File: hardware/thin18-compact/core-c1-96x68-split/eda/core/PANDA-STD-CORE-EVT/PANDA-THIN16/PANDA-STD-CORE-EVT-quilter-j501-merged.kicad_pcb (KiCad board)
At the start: 4 copper layers, 96 x 68 mm, 147 parts, among them J201 U20405-01 USB2.0, J301 HC-HY-2AWT, J302 HC-1.0-3PWT NTC, J501 TF-122-CCP9 / microSD, J502 HC-1.0-2PWT BTL, J503 TC2030-IDC-NL / DEBUG, J601 HC-PBB40C-60DS-0.4V-1.5-02, J803 X05A10H06G, J804 X05A10H06G, SW201 TS-1186E-B-B, SW202 TS-1186E-B-B, U302 SD3078, U402 SGM2578SDYG/TR, U403 SGM2578SDYG/TR, U404 SGM2578SDYG/TR, U405 SGM2578SDYG/TR, U501 ESP32-S3-WROOM-1U-N16R8, U503 QMI8658A, U601 XL9535, U901 SGM41513YTQF24G/TR, U902 SGM62125AXG/TR, U903 CW2217BAAD, U904 NS4168, U905 SGM37601YTRL20G/TR

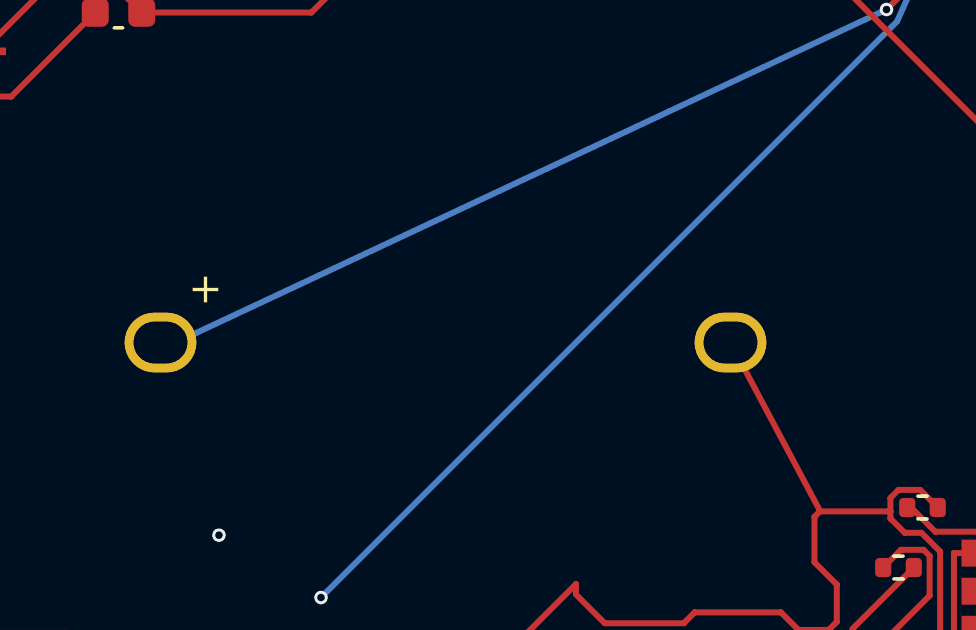
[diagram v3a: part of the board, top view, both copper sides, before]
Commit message: fix(hardware): use exact H3C capacitor with 20mm leads
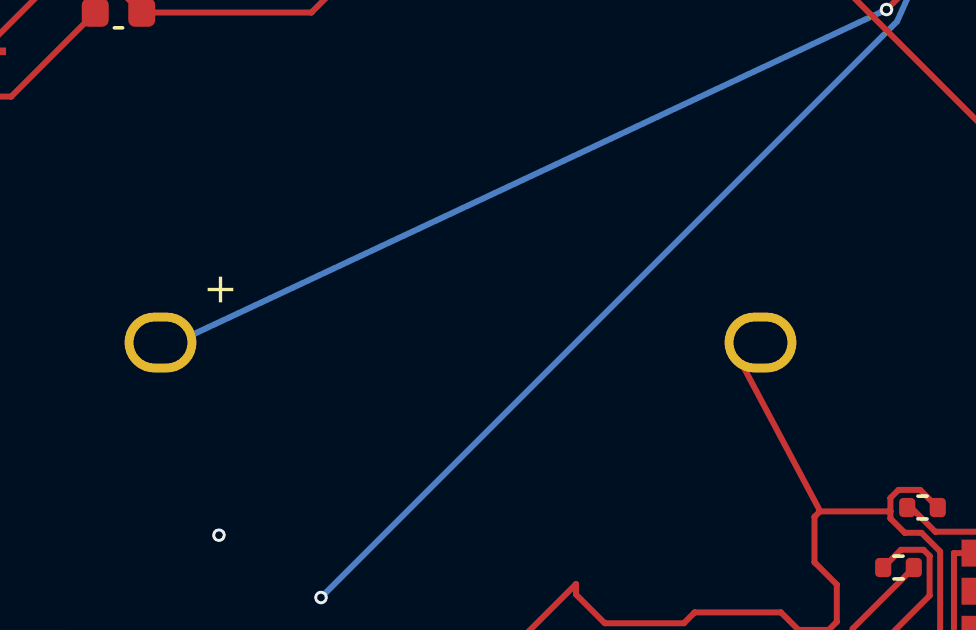
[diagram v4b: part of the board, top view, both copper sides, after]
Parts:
- C301: value SE-5R5-D105VYH -> SE-5R5-D105VYH3C; footprint panda-standard:KAMCAP_SE5R5_D105VYH -> panda-standard:KAMCAP_SE5R5_D105VYH3C
- moved C301 0.50 mm to (59.4, 43.5)
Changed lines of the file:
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@@
 (property "LCSC" "C22399626" (at 0 0 0) (layer "F.Fab") (hide yes) (effects (font (size 1.27 1.27))))(property "Manufacturer" "HRE" (at 0 0 0) (layer "F.Fab") (hide yes) (effects (font (size 1 1))))(property "MPN" "CGA0603X7R106K100JT" (at 0 0 0) (layer "F.Fab") (hide yes) (effects (font (size 1 1)))) (property "Description" "Controlled prototype ECO: HRE 10uF 10V X7R +/-10% 0603, C22399626; effective DC-bias capacitance remains a physical qualification item." (at 0 0 0) (layer "F.Fab") (hide yes) (effects (font (size 1.27 1.27)))) (property "KiLib_Generator" "SMD_2terminal_chip_molded" (at 0 0 0) (layer "F.SilkS") (hide yes) (effects (font (size 1 1) (thickness 0.15)))) (attr smd) (duplicate_pad_numbers_are_jumpers no) (fp_line (start -0.14058 -0.51) (end 0.14058 -0.51) (stroke (width 0.12) (type solid)) (layer "F.SilkS")) (fp_line (start -0.14058 0.51) (end 0.14058 0.51) (stroke (width 0.12) (type solid)) (layer "F.SilkS")) (fp_rect (start -1.48 -0.73) (end 1.48 0.73) (stroke (width 0.05) (type solid)) (fill no) (layer "F.CrtYd")) (fp_rect (start -0.8 -0.4) (end 0.8 0.4) (stroke (width 0.1) (type solid)) (fill no) (layer "F.Fab")) (fp_text user "${REFERENCE}" (at 0 0 0) (layer "F.Fab") (effects (font (size 0.4 0.4) (thickness 0.06)))) (pad "1" smd roundrect (at -0.775 0) (size 0.9 0.95) (layers "F.Cu" "F.Mask" "F.Paste") (roundrect_rratio 0.25) (net "3V3_SD")) (pad "2" smd roundrect (at 0.775 0) (size 0.9 0.95) (layers "F.Cu" "F.Mask" "F.Paste") (roundrect_rratio 0.25) (net "GND")) (embedded_fonts no) (model "${KICAD10_3DMODEL_DIR}/Capacitor_SMD.3dshapes/C_0603_1608Metric.step" (offset (xyz 0 0 0)) (scale (xyz 1 1 1)) (rotate (xyz 0 0 0))))
 	(footprint "Capacitor_SMD:C_0402_1005Metric" (locked yes) (layer "F.Cu") (at 44.75 15.25 -90) (descr "Capacitor SMD 0402 (1005 Metric), square (rectangular) end terminal, IPC-7351 nominal, (Body size source: IPC-SM-782 page 76, https://www.pcb-3d.com/wordpress/wp-content/uploads/ipc-sm-782a_amendment_1_and_2.pdf)") (tags "capacitor") (property "Reference" "C303" (at 0 1.8 90) (layer "F.SilkS") (hide yes) (effects (font (size 0.8 0.8) (thickness 0.12)))) (property "Value" "1u / BQ BAT" (at 0 1.16 90) (layer "F.Fab") (hide yes) (effects (font (size 1 1) (thickness 0.15)))) (property "Datasheet" "https://www.ti.com/lit/ds/symlink/bq27427.pdf" (at 0 0 90) (layer "F.Fab") (hide yes) (effects (font (size 1.27 1.27))))(property "Manufacturer" "FH (Fenghua Advanced)" (at 0 0 90) (layer "F.Fab") (hide yes) (effects (font (size 1 1))))(property "MPN" "0402B105K100NT" (at 0 0 90) (layer "F.Fab") (hide yes) (effects (font (size 1 1))))(property "LCSC" "C1526" (at 0 0 90) (layer "F.Fab") (hide yes) (effects (font (size 1 1)))) (property "Description" "BQ27427 BAT local ceramic bypass; 1 uF follows TI Table 4-1 and application sections; exact MPN, voltage and DC-bias pending controlled BOM review." (at 0 0 90) (layer "F.Fab") (hide yes) (effects (font (size 1.27 1.27)))) (property "KiLib_Generator" "SMD_2terminal_chip_molded" (at 0 0 90) (layer "F.SilkS") (hide yes) (effects (font (size 1 1) (thickness 0.15)))) (sheetname "/") (sheetfile "PANDA-STD-CORE-EVT.kicad_sch") (attr smd) (duplicate_pad_numbers_are_jumpers no) (fp_line (start -0.107836 0.36) (end 0.107836 0.36) (stroke (width 0.12) (type solid)) (layer "F.SilkS")) (fp_line (start -0.107836 -0.36) (end 0.107836 -0.36) (stroke (width 0.12) (type solid)) (layer "F.SilkS")) (fp_rect (start -0.91 -0.46) (end 0.91 0.46) (stroke (width 0.05) (type solid)) (fill no) (layer "F.CrtYd")) (fp_rect (start -0.5 -0.25) (end 0.5 0.25) (stroke (width 0.1) (type solid)) (fill no) (layer "F.Fab")) (fp_text user "${REFERENCE}" (at 0 0 90) (layer "F.Fab") (effects (font (size 0.25 0.25) (thickness 0.04)))) (pad "1" smd roundrect (at -0.48 0 270) (size 0.56 0.62) (layers "F.Cu" "F.Mask" "F.Paste") (roundrect_rratio 0.25) (net "BAT_PACKP")) (pad "2" smd roundrect (at 0.48 0 270) (size 0.56 0.62) (layers "F.Cu" "F.Mask" "F.Paste") (roundrect_rratio 0.25) (net "GND")) (embedded_fonts no) (model "${KICAD10_3DMODEL_DIR}/Capacitor_SMD.3dshapes/C_0402_1005Metric.step" (offset (xyz 0 0 0)) (scale (xyz 1 1 1)) (rotate (xyz 0 0 0))))
-	(footprint "panda-standard:KAMCAP_SE5R5_D105VYH" (locked yes) (layer "F.Cu") (at 58.9 43.5) (descr "KAMCAP SE-5R5-D105VYH primary2017:1F -20/+80%,5.5V,15ohm maxESR;maxbody19.2diameter/6.0height;leadpitch19+/-0.5,lead1.0+/-0.1. Engineering19mm pitch,platedslots1.8x1.4,lands2.4x2.0. Pin1=positive,2=GND:install actual marked+ terminal on PCB+;drawing has no numbered polarity view. Hand-solder after SMT;body must clear PCB0.2,cut lead belowCore B<=0.5. Prototype retention budget conditional on precharge/current;not physical validation.") (tags "KAMCAP SE-5R5-D105VYH horizontal THT rechargeable RTC backup") (property "Reference" "C301" (at 2.5 -12.3 90) (layer "F.SilkS") (hide yes) (effects (font (size 1 1) (thickness 0.15)))) (property "Value" "SE-5R5-D105VYH" (at 2.5 12.3 90) (layer "F.Fab") (effects (font (size 1 1) (thickness 0.15)))) (property "Datasheet" "https://atta.szlcsc.com/upload/public/pdf/source/20170717/C118887_1500269960558820748.pdf" (at 0 0 90) (layer "B.Fab") (hide yes) (effects (font (size 1.27 1.27))))
-(property "LCSC" "C118887" (at 0 0 90) (layer "B.Fab") (hide yes) (effects (font (size 1.27 1.27))))(property "Manufacturer" "KAMCAP" (at 0 0 90) (layer "B.Fab") (hide yes) (effects (font (size 1 1))))(property "MPN" "SE-5R5-D105VYH" (at 0 0 90) (layer "B.Fab") (hide yes) (effects (font (size 1 1)))) (property "Description" "KAMCAP SE-5R5-D105VYH primary2017:1F -20/+80%,5.5V,15ohm maxESR;maxbody19.2diameter/6.0height;leadpitch19+/-0.5,lead1.0+/-0.1. Engineering19mm pitch,platedslots1.8x1.4,lands2.4x2.0. Pin1=positive,2=GND:install actual marked+ terminal on PCB+;drawing has no numbered polarity view. Hand-solder after SMT;body must clear PCB0.2,cut lead belowCore B<=0.5. Prototype retention budget conditional on precharge/current;not physical validation." (at 0 0 90) (layer "B.Fab") (hide yes) (effects (font (size 1.27 1.27)))) (property "KiLib_Generator" "SMD_2terminal_chip_molded" (at 0 0 90) (layer "F.SilkS") (hide yes) (effects (font (size 1 1) (thickness 0.15)))) (attr through_hole) (duplicate_pad_numbers_are_jumpers no)        (embedded_fonts no)
-(fp_rect (start -10.95 -9.85) (end 10.95 9.85) (stroke (width 0.05) (type solid)) (fill no) (layer "F.CrtYd"))
+	(footprint "panda-standard:KAMCAP_SE5R5_D105VYH3C" (locked yes) (layer "F.Cu") (at 59.4 43.5) (descr "KAMCAP SE-5R5-D105VYH3C primaryJune2020 p3-4:1F 0/+30% at4.4..2.75V,5.5V,15ohm maxAC ESR;maxbody19.2diameter/6.5height;pitch20+/-0.5;flatleads width1.0+/-0.1,thickness0.2+/-0.05. Engineering20mm pitch,platedslots1.8x1.4,lands2.4x2.0. Pin1=positive,2=GND;marked negative terminal to pad2,other positive to PCB+. Post-SMT manual solder only;primary260C<=5s based1.6mm PCB,0.8mmCore process needs qualification;bodyclearance0.2,trimrearleads<=0.5. Conditional24h budget;leakage/low-voltage capacitance/physical EVT not qualified.") (tags "KAMCAP SE-5R5-D105VYH3C horizontal THT rechargeable RTC backup") (property "Reference" "C301" (at 2.5 -12.3 90) (layer "F.SilkS") (hide yes) (effects (font (size 1 1) (thickness 0.15)))) (property "Value" "SE-5R5-D105VYH3C" (at 2.5 12.3 90) (layer "F.Fab") (effects (font (size 1 1) (thickness 0.15)))) (property "Datasheet" "https://atta.szlcsc.com/upload/public/pdf/source/20210914/37A5D1176C23A52D8BA2A343DB47BCB6.pdf" (at 0 0 90) (layer "B.Fab") (hide yes) (effects (font (size 1.27 1.27))))
+(property "LCSC" "C2894294" (at 0 0 90) (layer "B.Fab") (hide yes) (effects (font (size 1.27 1.27))))(property "Manufacturer" "KAMCAP" (at 0 0 90) (layer "B.Fab") (hide yes) (effects (font (size 1 1))))(property "MPN" "SE-5R5-D105VYH3C" (at 0 0 90) (layer "B.Fab") (hide yes) (effects (font (size 1 1)))) (property "Description" "KAMCAP SE-5R5-D105VYH3C primaryJune2020 p3-4:1F 0/+30% at4.4..2.75V,5.5V,15ohm maxAC ESR;maxbody19.2diameter/6.5height;pitch20+/-0.5;flatleads width1.0+/-0.1,thickness0.2+/-0.05. Engineering20mm pitch,platedslots1.8x1.4,lands2.4x2.0. Pin1=positive,2=GND;marked negative terminal to pad2,other positive to PCB+. Post-SMT manual solder only;primary260C<=5s based1.6mm PCB,0.8mmCore process needs qualification;bodyclearance0.2,trimrearleads<=0.5. Conditional24h budget;leakage/low-voltage capacitance/physical EVT not qualified." (at 0 0 90) (layer "B.Fab") (hide yes) (effects (font (size 1.27 1.27)))) (property "KiLib_Generator" "SMD_2terminal_chip_molded" (at 0 0 90) (layer "F.SilkS") (hide yes) (effects (font (size 1 1) (thickness 0.15)))) (attr through_hole) (duplicate_pad_numbers_are_jumpers no)        (embedded_fonts no)
+(fp_rect (start -11.45 -9.85) (end 11.45 9.85) (stroke (width 0.05) (type solid)) (fill no) (layer "F.CrtYd"))
 (fp_circle (center 0 0) (end 9.6 0) (stroke (width 0.1) (type solid)) (fill no) (layer "F.Fab"))
-(pad "1" thru_hole oval (at -9.5 0) (size 2.4 2.0) (drill oval 1.8 1.4) (layers "*.Cu" "*.Mask") (net "RTC_VBACKUP") (pinfunction "+") (pintype "passive"))
-(pad "2" thru_hole oval (at 9.5 0) (size 2.4 2.0) (drill oval 1.8 1.4) (layers "*.Cu" "*.Mask") (net "GND") (pinfunction "-") (pintype "passive"))
+(pad "1" thru_hole oval (at -10 0) (size 2.4 2.0) (drill oval 1.8 1.4) (layers "*.Cu" "*.Mask") (net "RTC_VBACKUP") (pinfunction "+") (pintype "passive"))
+(pad "2" thru_hole oval (at 10 0) (size 2.4 2.0) (drill oval 1.8 1.4) (layers "*.Cu" "*.Mask") (net "GND") (pinfunction "-") (pintype "passive"))
 (fp_text user "+" (at -8 -1.8 0) (layer "F.SilkS") (effects (font (size 1 1) (thickness 0.15))))
 )

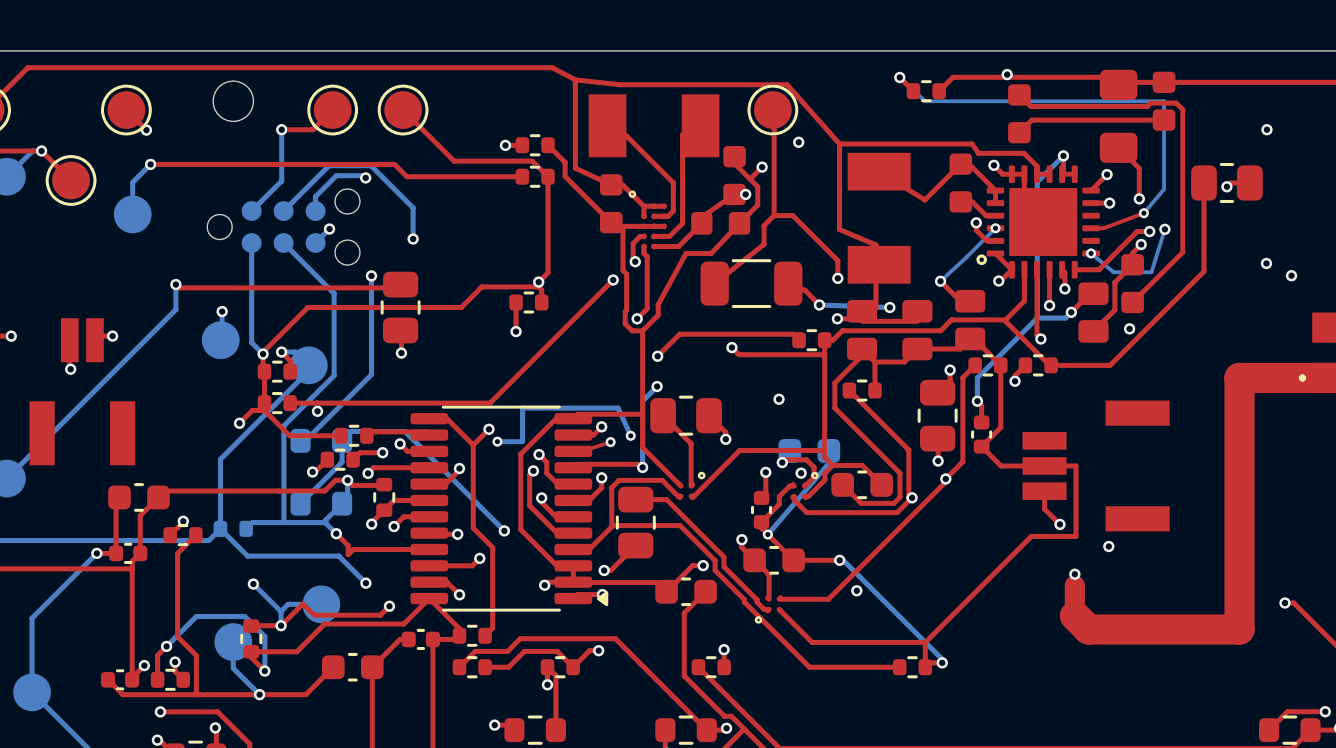
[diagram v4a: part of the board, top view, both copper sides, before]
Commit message: hw: implement Split-C1 PG monitor and pre-AON PSEL bias
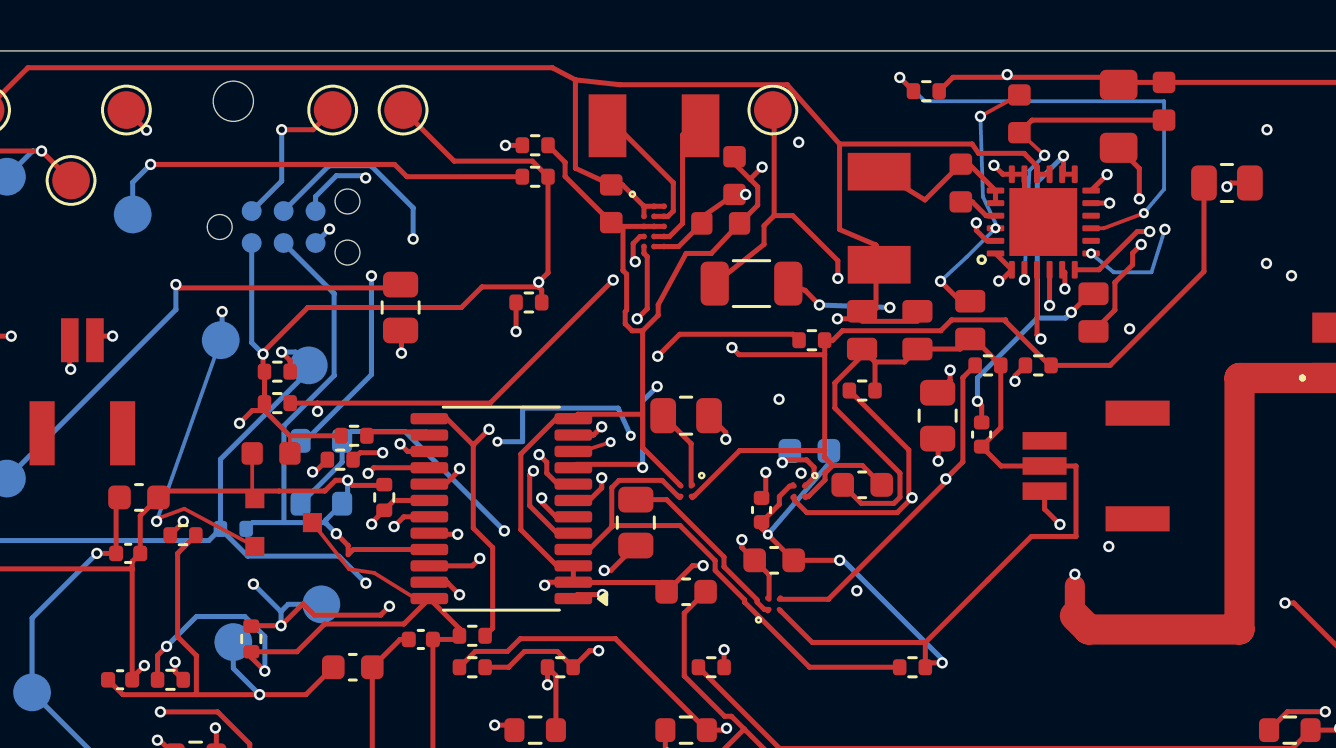
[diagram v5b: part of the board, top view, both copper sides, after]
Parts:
- added U906: SGM809B-TXN3LG/TR, panda-standard:SGM809B_SOT23_TX00031, F.Cu at (17.0, 18.8)
- C204: value 330n / ILIM-RC -> 330n / U906 bypass
- R201: value 5.6k / ILIM -> 5.6k / PSEL low leg
- R204: value 1.2k / ILIM-RC -> 1.2k / REGN to PSEL
- moved C204 34.9 mm to (16.5, 16.0), turned to 180 degrees
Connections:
- C204 pad 1: BQ_ILIM_RC -> 3V3_AON
- R201 pad 1: BQ_ILIM -> SGM41513_PSEL
- R204 pad 1: BQ_ILIM -> SGM41513_PSEL
- R204 pad 2: BQ_ILIM_RC -> SGM41513_REGN
- U901 pad 2: 3V3_AON -> SGM41513_PSEL
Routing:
- net BQ_ILIM_RC: track 15.3 -> 0.00 mm
- net SGM41513_PSEL: track 0.00 -> 12.4 mm, vias 0 -> 2
- net PG_3V3_MAIN: track 16.4 -> 27.7 mm, vias 2 -> 3
- net SGM41513_REGN: track 35.6 -> 41.8 mm, vias 3 -> 4
- net BQ_ILIM: track 5.96 -> 0.00 mm
- net 3V3_AON: track 341.9 -> 345.2 mm
- net GND: track 757.4 -> 758.8 mm

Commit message: hw: finish Split-C1 default-off charging and direct GPIO inhibit
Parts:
- added Q907: NX3008NBK,215-JSM, panda-standard:JSM_NX3008NBK_SOT23, F.Cu at (53.2, 8.25)
- added Q908: NX3008NBK,215-JSM, panda-standard:JSM_NX3008NBK_SOT23, F.Cu at (52.8, 11.8)
- added R930: 100k / nCE default OFF, Resistor_SMD:R_0402_1005Metric, F.Cu at (51.8, 5.25)
- added R931: 1.2k / hardware permit, panda-standard:R204_ILIM_RC_0603_SEED, F.Cu at (73.5, 66.0)
- added R932: 10k / gate default LOW, Resistor_SMD:R_0402_1005Metric, F.Cu at (51.0, 9.00)
- added R933: 10k / gate default LOW, Resistor_SMD:R_0402_1005Metric, F.Cu at (55.2, 11.2)
- added TP19: HW_ARM / FORCE LOW, TestPoint:TestPoint_Pad_D1.5mm, B.Cu at (58.0, 17.0)
- R607: value 100k / BQ_CE_PD -> 100k / CHG_REQUEST_PD
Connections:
- R607 pad 1: BQ_CE -> CHG_REQUEST
- U501 pad 38: unconnected-(U501-IO2-Pad38) -> HW_ARM_GPIO
- U601 pad 18: FL_HWEN -> unconnected-(U601-P15-Pad18)
- U601 pad 9: BQ_CE -> CHG_REQUEST
- U901 pad 9: BQ_CE -> CHG_nCE
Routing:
- net FL_HWEN: track 41.9 -> 157.0 mm, vias 2 -> 6
- net CHG_REQUEST: track 0.00 -> 47.9 mm, vias 0 -> 5
- net BQ_CE: track 41.2 -> 0.00 mm, vias 4 -> 0
- net CHG_nCE: track 0.00 -> 15.7 mm, vias 0 -> 3
- net CHG_RETURN: track 0.00 -> 15.5 mm
- net GND: track 758.8 -> 769.4 mm
- net SGM41513_REGN: track 41.8 -> 50.6 mm
- net HW_ARM_GPIO: track 0.00 -> 3.53 mm, vias 0 -> 2
